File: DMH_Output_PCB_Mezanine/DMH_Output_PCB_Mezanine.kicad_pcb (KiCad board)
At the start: 2 copper layers, 49 x 164.5 mm, 105 parts, among them J30 Conn_01x04_PinHeader, J32 Conn_01x06_PinHeader, J33 Conn_01x06, J34 Conn_01x06, J37 Conn_01x06, J38 Conn_01x06, J39 Conn_01x02_PinHeader, J40 Conn_01x02_PinHeader, U10 NE5532, U16 NE5532, U17 NE5532, U18 NE5532, U19 NE5532, U7 TL072, U9 NE5532

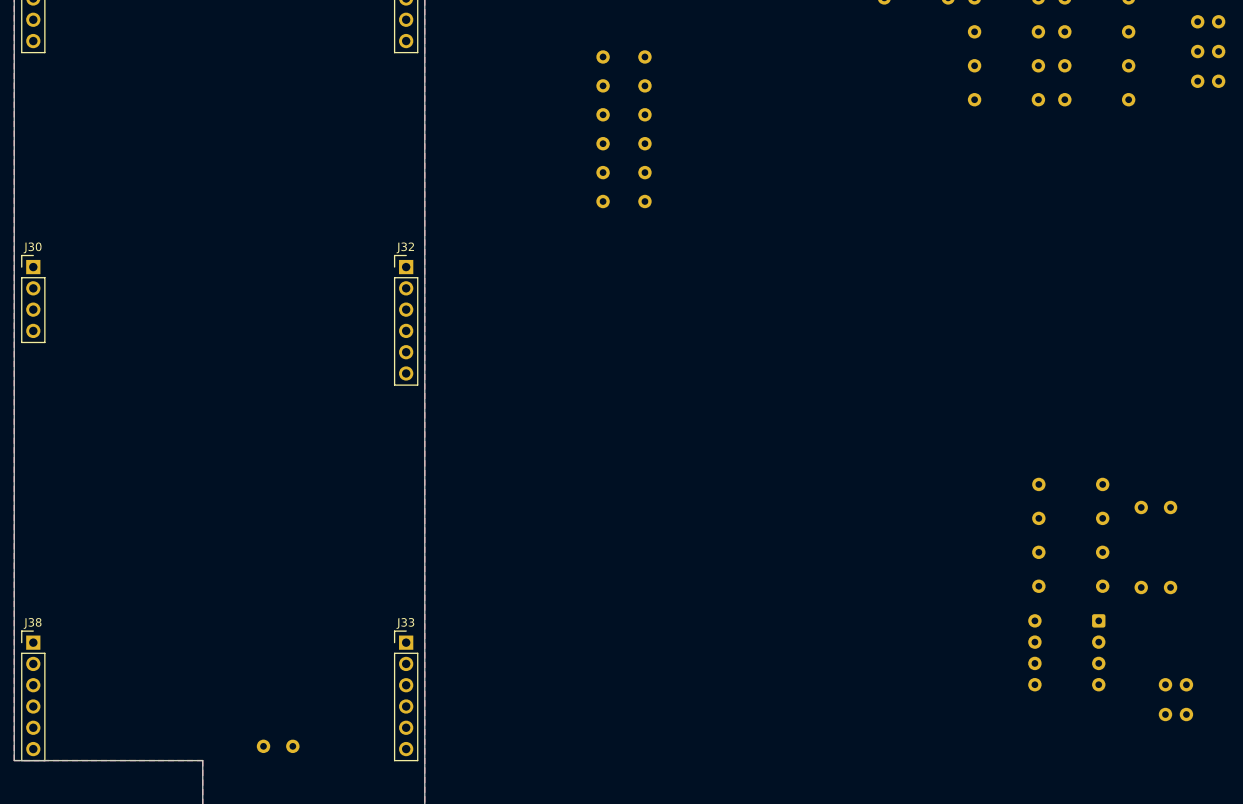
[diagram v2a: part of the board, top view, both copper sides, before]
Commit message: Placed pre-gain stage components
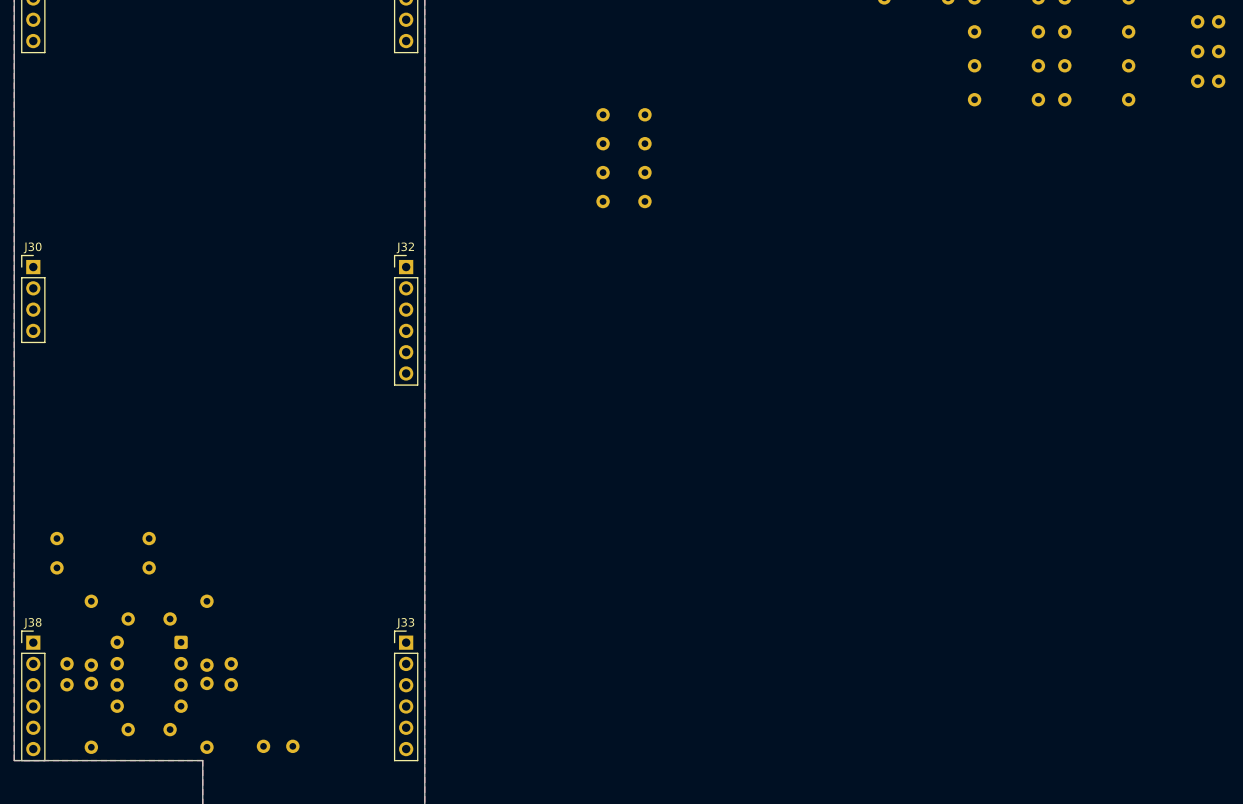
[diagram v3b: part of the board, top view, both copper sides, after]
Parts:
- moved C9 133.7 mm to (56.8, 141.4), turned to -90 degrees
- moved C10 132.9 mm to (55.6, 130.0), turned to 90 degrees
- moved R28 122.9 mm to (59.7, 151.4), turned to 90 degrees
- moved C7 122.1 mm to (66.6, 130.0), turned to 90 degrees
- moved R29 120.7 mm to (59.7, 134.0), turned to -90 degrees
- moved C8 114.0 mm to (76.4, 141.4), turned to -90 degrees
- moved R27 110.3 mm to (73.5, 151.4), turned to 90 degrees
- moved U7 109.6 mm to (70.4, 138.9)
- moved R26 107.8 mm to (73.5, 134.0), turned to -90 degrees
- moved C55 98.5 mm to (64.1, 149.3), turned to 0 degrees
- moved C53 91.1 mm to (64.1, 136.1), turned to 0 degrees

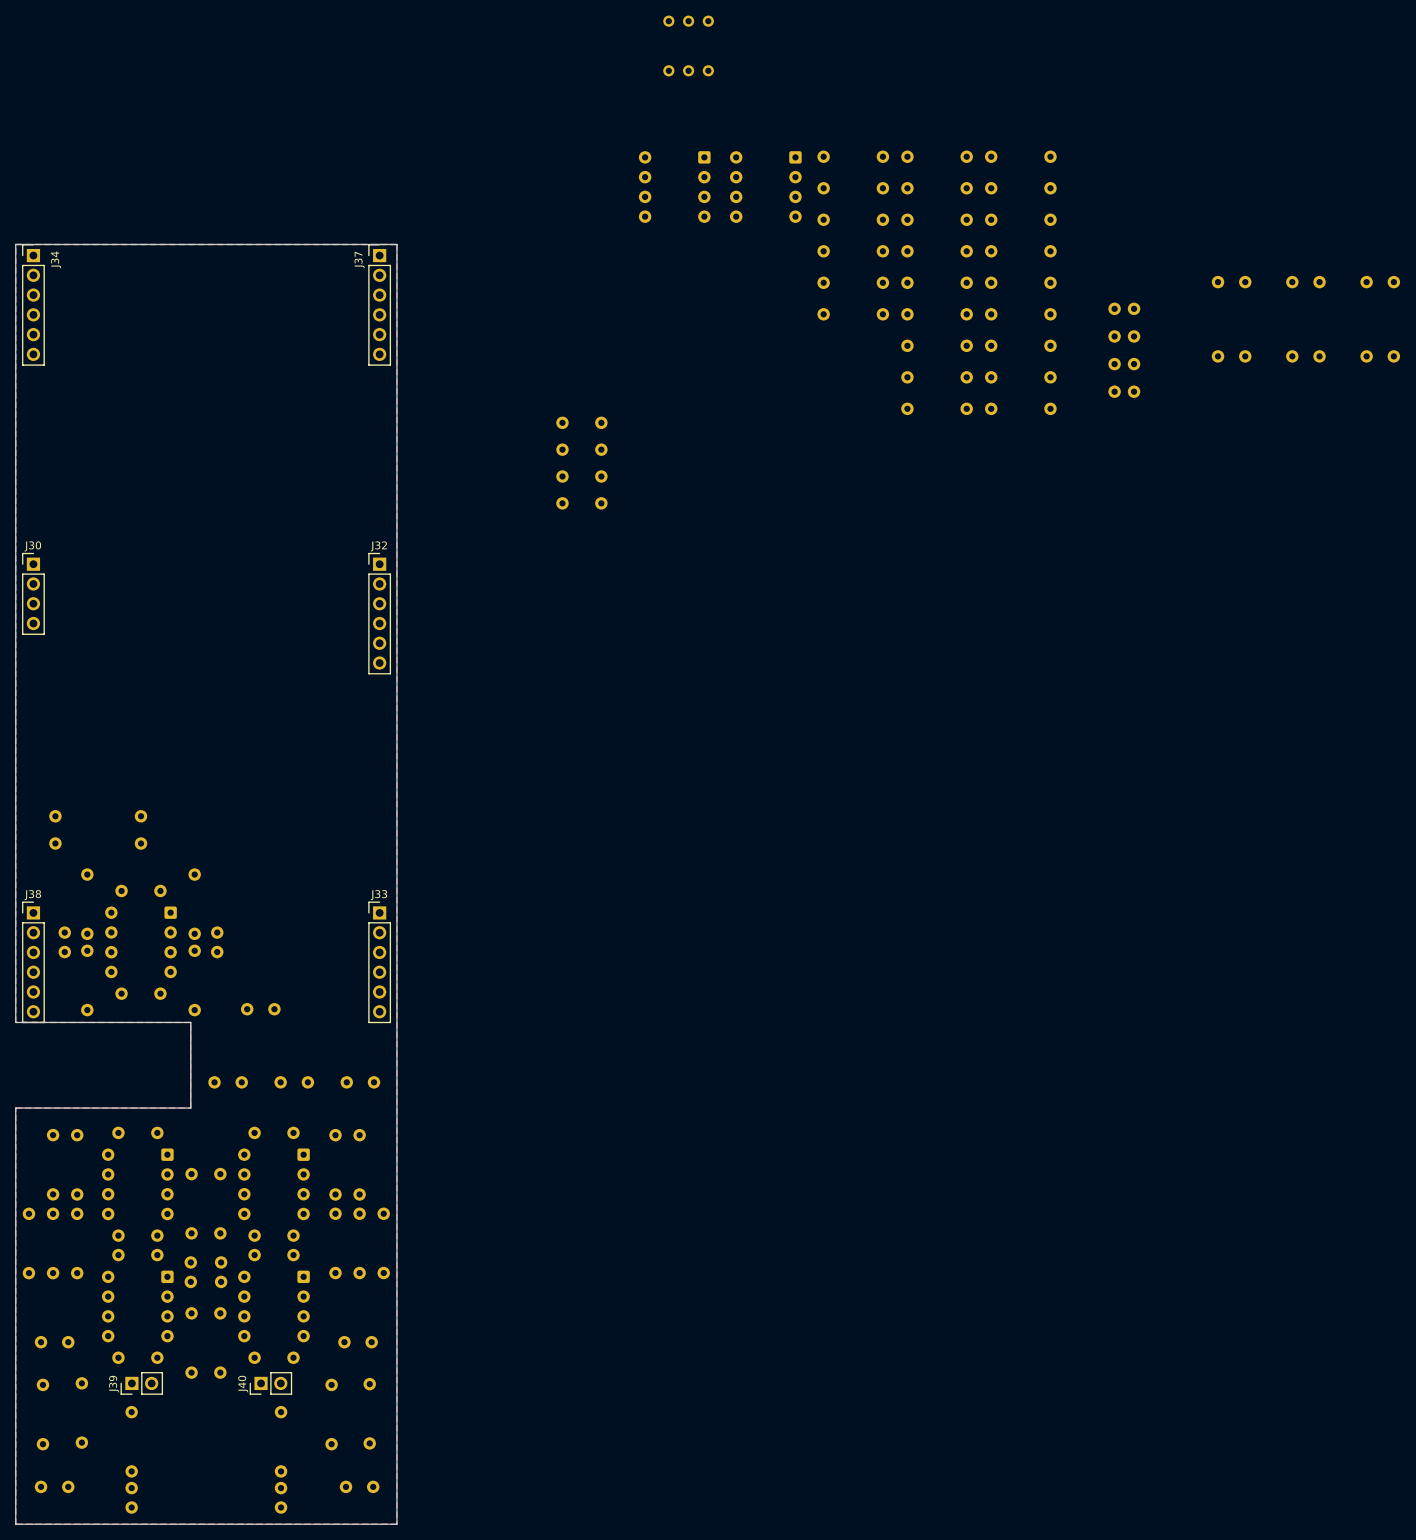
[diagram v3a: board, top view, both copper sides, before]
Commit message: Mezanine PCB comp placement done
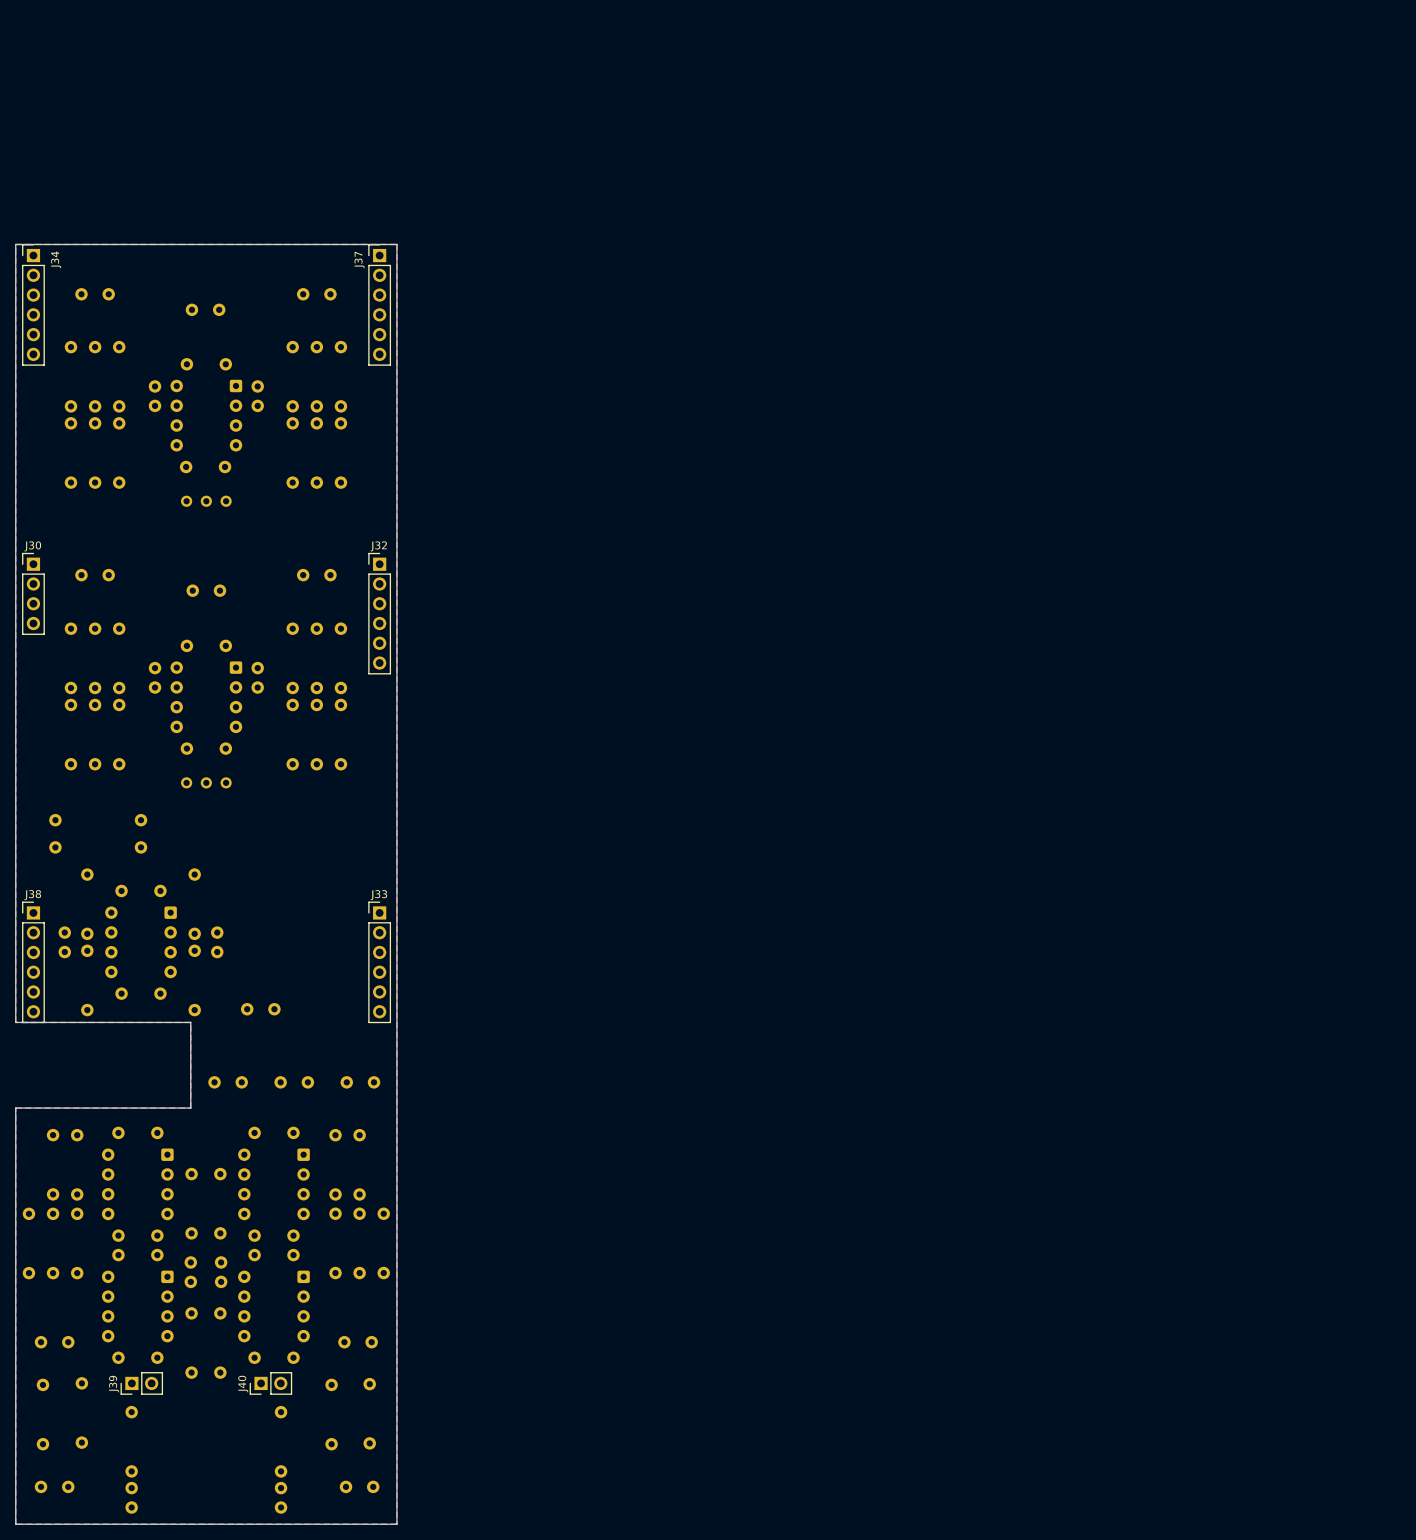
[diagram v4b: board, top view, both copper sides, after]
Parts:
- C25, C26, C30, C33: value 22pF 50V -> 22pF
- moved C28 168.9 mm to (59.0, 59.4), turned to 0 degrees
- moved C34 152.2 mm to (59.0, 95.5), turned to 0 degrees
- moved C27 151.0 mm to (76.7, 61.4)
- moved C31 144.5 mm to (76.8, 97.5)
- moved R43 135.0 mm to (57.6, 112.2), turned to -90 degrees
- moved C33 131.5 mm to (68.4, 110.0), turned to 90 degrees
- moved C29 127.1 mm to (91.0, 59.4)
- moved R38 126.2 mm to (57.6, 66.2), turned to -90 degrees
- moved C26 126.2 mm to (68.4, 73.8), turned to 90 degrees
- moved R35 125.5 mm to (63.8, 83.6), turned to 90 degrees
- moved C32 123.5 mm to (91.0, 95.5)
- moved R36 122.1 mm to (63.8, 73.8), turned to 90 degrees
- moved R112 120.6 mm to (63.8, 119.8), turned to 90 degrees
- moved C30 120.1 mm to (81.6, 110.0), turned to 90 degrees
- moved R107 119.6 mm to (63.8, 110.0), turned to 90 degrees
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
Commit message: routing ongoing
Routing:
- net -12V: track 0.00 -> 163.5 mm
- net +12V: track 0.00 -> 156.2 mm

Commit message: routing in progress
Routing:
- net /PreAmp/RV3A_p1_MZ: track 0.00 -> 93.4 mm
- net Net-(J32C-Pin_3): track 0.00 -> 85.9 mm
- net +12V: track 156.2 -> 225.6 mm
- net Net-(J32F-Pin_6): track 0.00 -> 65.5 mm
- net Net-(J32D-Pin_4): track 0.00 -> 62.3 mm
- net /PreAmp/RV3B_p4_MZ: track 0.00 -> 62.1 mm
- net Net-(J32E-Pin_5): track 0.00 -> 59.5 mm
- net -12V: track 163.5 -> 219.0 mm
- net Net-(J30B-Pin_2): track 0.00 -> 51.9 mm
- net Net-(C29-Pad2): track 0.00 -> 43.7 mm
- net Net-(J30A-Pin_1): track 0.00 -> 42.8 mm
- net Net-(J32B-Pin_2): track 0.00 -> 39.9 mm
- net Net-(C32-Pad2): track 0.00 -> 39.5 mm
- net Net-(U16B-+): track 0.00 -> 37.5 mm
- net Net-(J30C-Pin_3): track 0.00 -> 37.3 mm
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
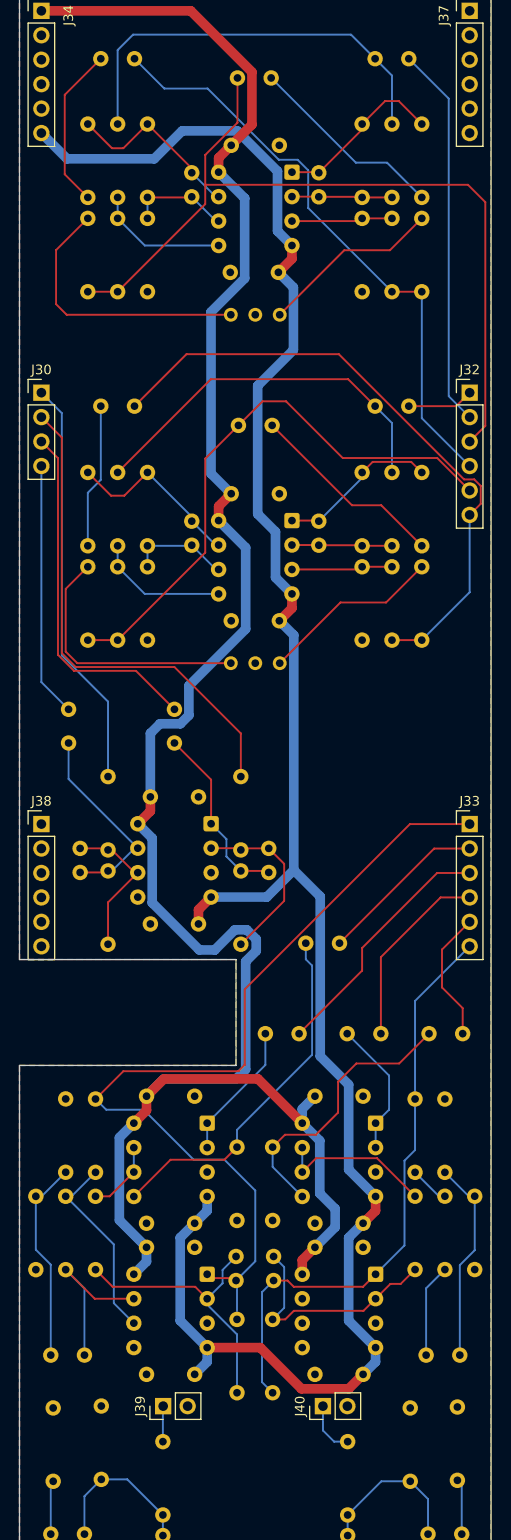
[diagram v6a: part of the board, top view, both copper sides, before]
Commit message: Mezanine PCB routing done
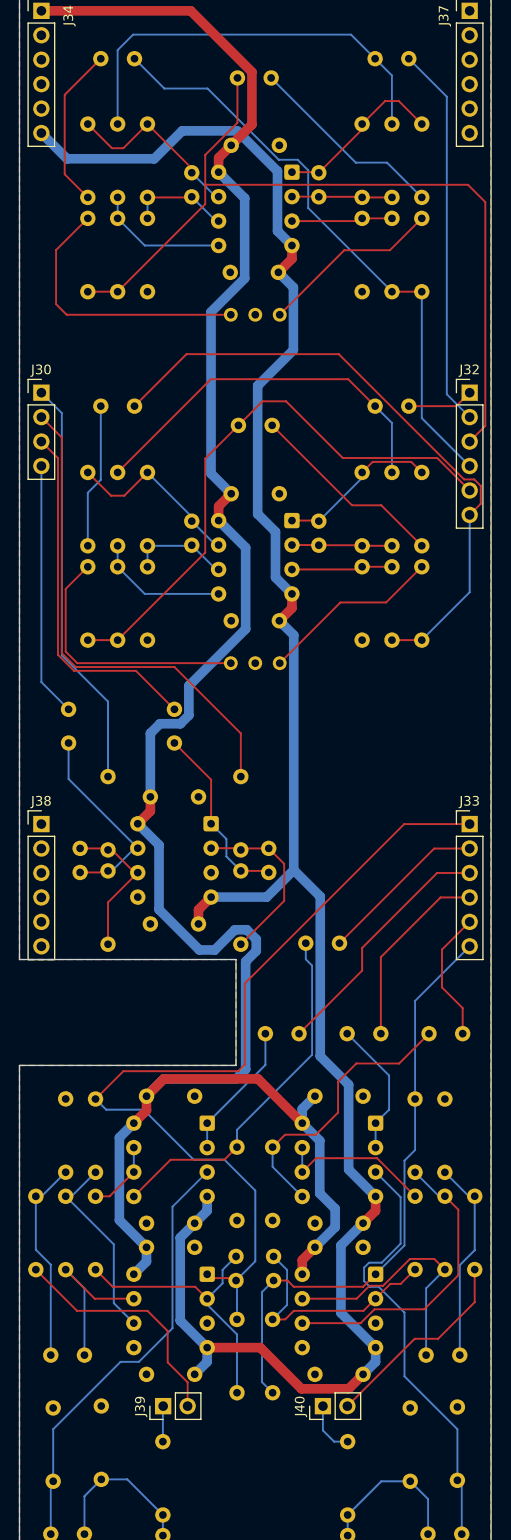
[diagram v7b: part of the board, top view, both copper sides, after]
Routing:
- net Net-(U18A-+): track 5.78 -> 45.8 mm
- net Net-(U16A-+): track 5.59 -> 45.5 mm
- net Net-(U19B--): track 4.13 -> 31.2 mm
- net Net-(J39B-Pin_2): track 0.00 -> 25.0 mm
- net Net-(J40B-Pin_2): track 0.00 -> 21.1 mm
- net Net-(C36-Pad1): track 9.70 -> 26.7 mm
- net -12V: track 219.0 -> 219.7 mm
